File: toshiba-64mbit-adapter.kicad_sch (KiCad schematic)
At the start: 12 parts, among them U1 TC5364205, U2 W29GL064C, U3 74LVC244, U4 74LVC244, U5 74LVC244, U6 74LVC244, U7 74LVC244, U8 TPS73633DBV

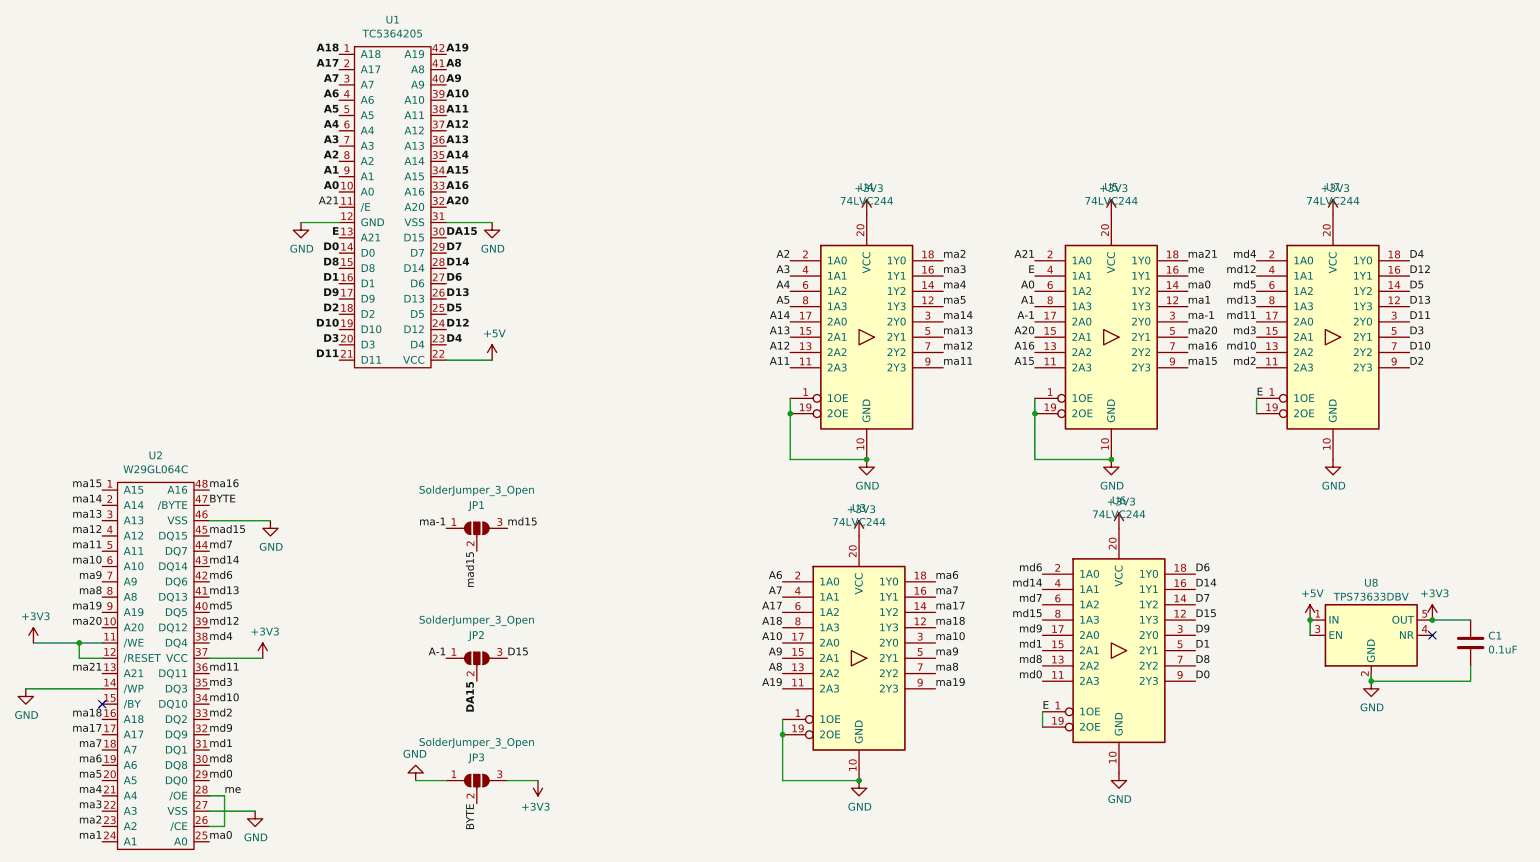
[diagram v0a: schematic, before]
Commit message: Switch the 2x data line LVC244s to HCT244s
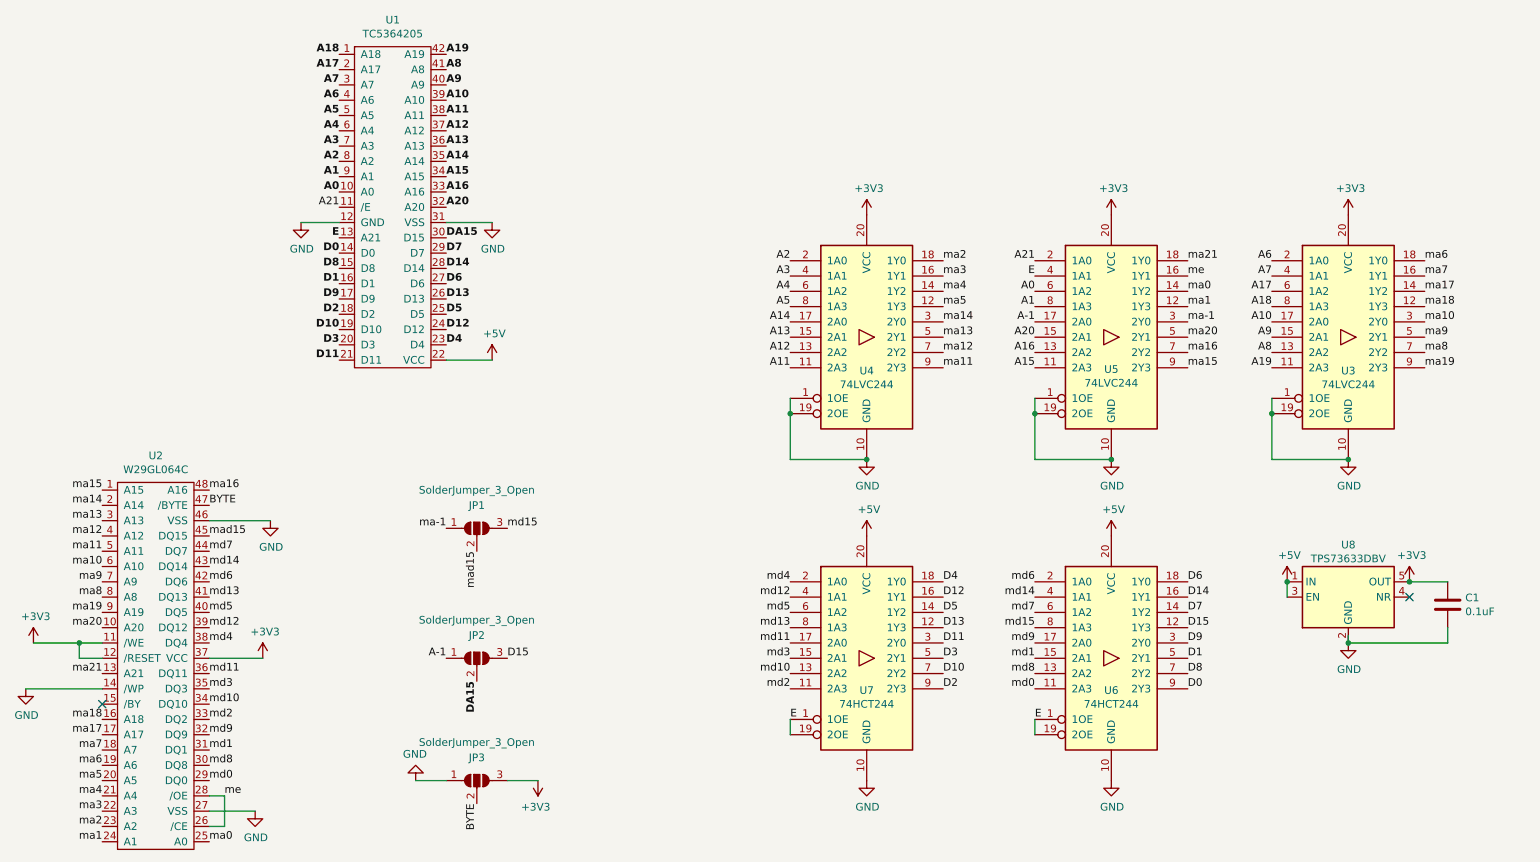
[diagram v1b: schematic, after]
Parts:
- U6, U7: value 74LVC244 -> 74HCT244
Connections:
- net +3V3: no longer U6.20 (VCC), U7.20 (VCC)
- net +5V: now also U6.20 (VCC), U7.20 (VCC)
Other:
- moved on the sheet: C1, U3, U6, U7, U8
